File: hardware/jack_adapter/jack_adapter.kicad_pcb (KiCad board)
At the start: 2 copper layers, 25.5 x 22 mm, 3 parts, among them J1 2.5mm Mic, J3 3.5mm Headphones, J4 Conn_01x03

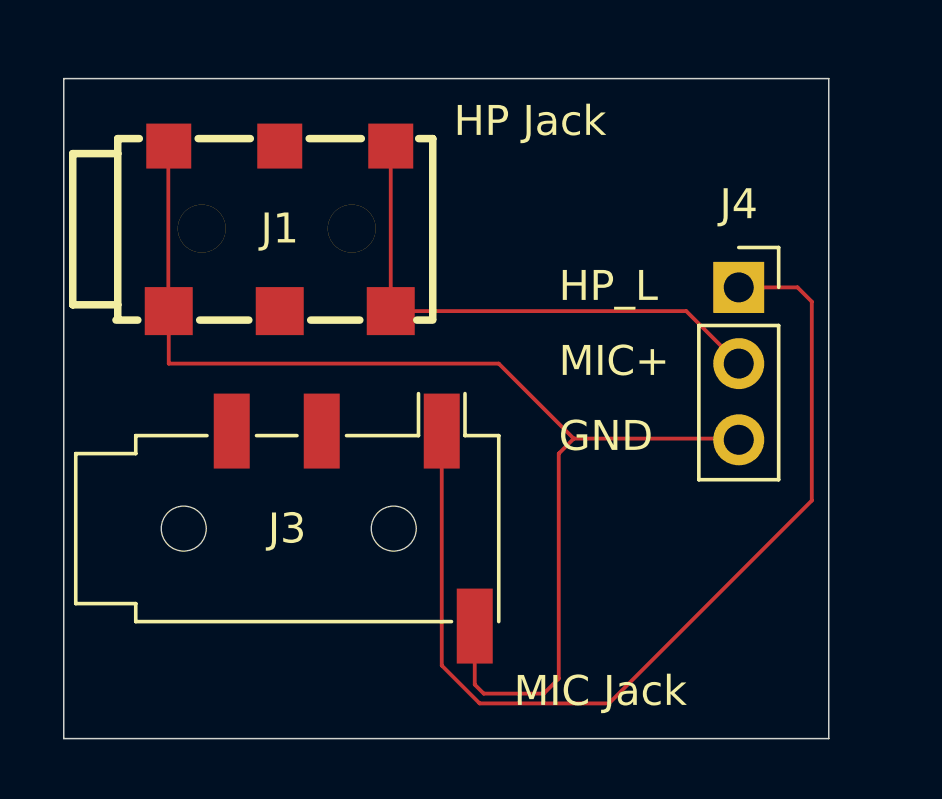
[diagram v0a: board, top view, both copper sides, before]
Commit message: feat: Add audio test circuit and board
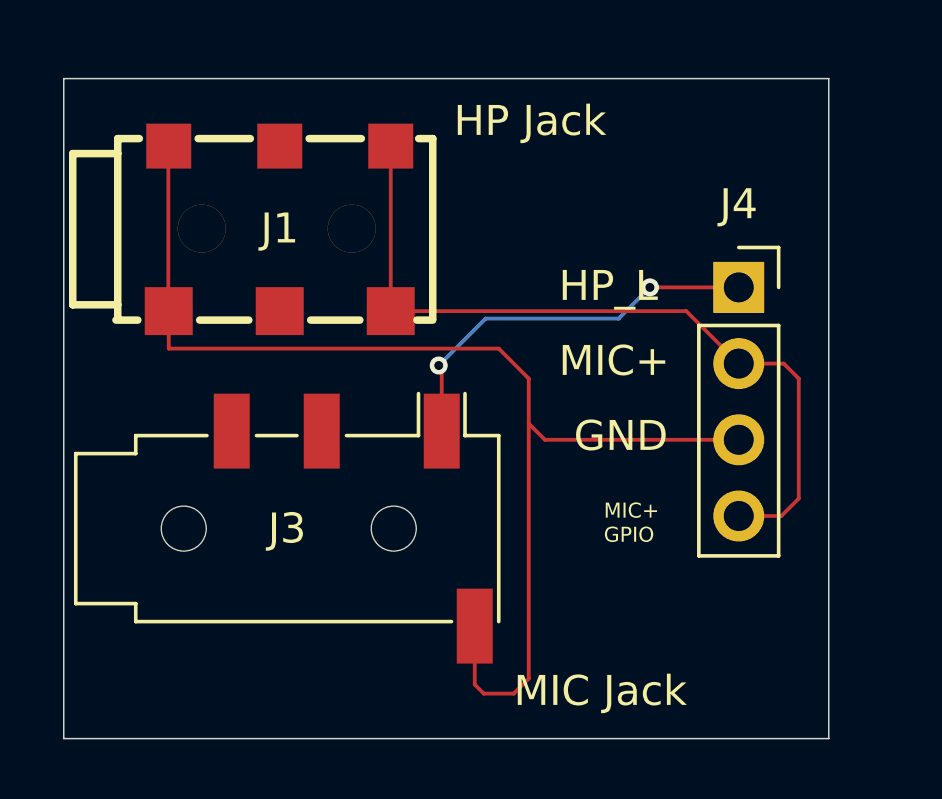
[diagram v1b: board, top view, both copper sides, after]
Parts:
- J4: footprint Connector_PinSocket_2.54mm:PinSocket_1x03_P2.54mm_Vertical -> Connector_PinSocket_2.54mm:PinSocket_1x04_P2.54mm_Vertical
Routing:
- net Net-(J4-Pin_1): track 32.7 -> 13.3 mm, vias 0 -> 2
- net Net-(J4-Pin_2): track 17.8 -> 26.3 mm
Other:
- board text added: "MIC+ GPIO"
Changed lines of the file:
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@@
 		)
 	)
-	(footprint "Connector_PinSocket_2.54mm:PinSocket_1x03_P2.54mm_Vertical"
+	(footprint "Connector_PinSocket_2.54mm:PinSocket_1x04_P2.54mm_Vertical"
 		(layer "F.Cu")
 		(at 37.5 21.96)
-		(descr "Through hole straight socket strip, 1x03, 2.54mm pitch, single row (from Kicad 4.0.7), script generated")
-		(tags "Through hole socket strip THT 1x03 2.54mm single row")
+		(descr "Through hole straight socket strip, 1x04, 2.54mm pitch, single row (from Kicad 4.0.7), script generated")
+		(tags "Through hole socket strip THT 1x04 2.54mm single row")
 		(property "Reference" "J4"
 			(at 0 -2.77 0)
@@
 		)
 		(property "Value" "Conn_01x03"
-			(at 0 7.85 0)
+			(at 0 10.39 0)
 			(layer "F.Fab")
 			(effects
@@
 			)
 		)
-		(property "Description" "Generic connector, single row, 01x03, script generated (kicad-library-utils/schlib/autogen/connector/)"
+		(property "Description" "Generic connector, single row, 01x04, script generated (kicad-library-utils/schlib/autogen/connector/)"
 			(at 0 0 0)
 			(layer "F.Fab")
@@
 		(fp_line
 			(start -1.33 1.27)
-			(end -1.33 6.41)
+			(end -1.33 8.95)
 			(stroke
 				(width 0.12)
@@
 		)
 		(fp_line
-			(start -1.33 6.41)
-			(end 1.33 6.41)
+			(start -1.33 8.95)
+			(end 1.33 8.95)
 			(stroke
 				(width 0.12)
@@
 		(fp_line
 			(start 1.33 1.27)
-			(end 1.33 6.41)
+			(end 1.33 8.95)
 			(stroke
 				(width 0.12)
@@
 		)
 		(fp_line
-			(start -1.8 6.85)
+			(start -1.8 9.4)
 			(end -1.8 -1.8)
 			(stroke
@@
 		(fp_line
 			(start 1.75 -1.8)
-			(end 1.75 6.85)
+			(end 1.75 9.4)
 			(stroke
 				(width 0.05)
@@
 		)
 		(fp_line
-			(start 1.75 6.85)
-			(end -1.8 6.85)
+			(start 1.75 9.4)
+			(end -1.8 9.4)
 			(stroke
 				(width 0.05)
@@
 		)
 		(fp_line
-			(start -1.27 6.35)
+			(start -1.27 8.89)
 			(end -1.27 -1.27)
 			(stroke
@@
 		(fp_line
 			(start 1.27 -0.635)
-			(end 1.27 6.35)
+			(end 1.27 8.89)
 			(stroke
 				(width 0.1)
@@
 		)
 		(fp_line
-			(start 1.27 6.35)
-			(end -1.27 6.35)
+			(start 1.27 8.89)
+			(end -1.27 8.89)
 			(stroke
 				(width 0.1)
@@
 		)
 		(fp_text user "${REFERENCE}"
-			(at 0 2.54 90)
+			(at 0 3.81 90)
 			(layer "F.Fab")
 			(effects
@@
 			(pintype "passive")
 		)
+		(pad "4" thru_hole circle
+			(at 0 7.62)
+			(size 1.7 1.7)
+			(drill 1)
+			(layers "*.Cu" "*.Mask")
+			(remove_unused_layers no)
+			(net 3 "Net-(J4-Pin_2)")
+			(pinfunction "Pin_4")
+			(pintype "passive")
+		)
 		(embedded_fonts no)
-		(model "${KICAD9_3DMODEL_DIR}/Connector_PinSocket_2.54mm.3dshapes/PinSocket_1x03_P2.54mm_Vertical.step"
+		(model "${KICAD9_3DMODEL_DIR}/Connector_PinSocket_2.54mm.3dshapes/PinSocket_1x04_P2.54mm_Vertical.step"
 			(offset
 				(xyz 0 0 0)
@@
 	)
 	(gr_text "GND"
-		(at 31.5 27.5 0)
+		(at 32 27.5 0)
 		(layer "F.SilkS")
 		(effects
@@
 		)
 	)
-	(segment
-		(start 32 27)
-		(end 37.46 27)
-		(width 0.127)
-		(layer "F.Cu")
-		(net 1)
-	)
-	(segment
-		(start 18.5 22.75)
-		(end 18.5 24.5)
+	(gr_text "MIC+\nGPIO"
+		(at 33 30.5 0)
+		(layer "F.SilkS")
+		(effects
+			(font
+				(size 0.5 0.5)
+				(thickness 0.1)
+			)
+			(justify left bottom)
+		)
+	)
+	(segment
+		(start 29.5 24)
+		(end 30.5 25)
+		(width 0.127)
+		(layer "F.Cu")
+		(net 1)
+	)
+	(segment
+		(start 30.5 35)
+		(end 30.5 26.5)
+		(width 0.127)
+		(layer "F.Cu")
+		(net 1)
+	)
+	(segment
+		(start 30 35.5)
+		(end 30.5 35)
 		(width 0.127)
 		(layer "F.Cu")
@@
 	)
 	(segment
+		(start 18.5 24)
+		(end 29.5 24)
+		(width 0.127)
+		(layer "F.Cu")
+		(net 1)
+	)
+	(segment
+		(start 18.5 22.75)
+		(end 18.5 24)
+		(width 0.127)
+		(layer "F.Cu")
+		(net 1)
+	)
+	(segment
 		(start 37.46 27)
 		(end 37.5 27.04)
@@
 	)
 	(segment
-		(start 18.5 24.5)
-		(end 29.5 24.5)
+		(start 28.7 33.25)
+		(end 28.7 35.2)
+		(width 0.127)
+		(layer "F.Cu")
+		(net 1)
+	)
+	(segment
+		(start 29 35.5)
+		(end 30 35.5)
+		(width 0.127)
+		(layer "F.Cu")
+		(net 1)
+	)
+	(segment
+		(start 37.5 27.04)
+		(end 31.04 27.04)
+		(width 0.127)
+		(layer "F.Cu")
+		(net 1)
+	)
+	(segment
+		(start 30.5 25)
+		(end 30.5 26.5)
+		(width 0.127)
+		(layer "F.Cu")
+		(net 1)
+	)
+	(segment
+		(start 18.4855 17.2645)
+		(end 18.4855 22.7355)
+		(width 0.127)
+		(layer "F.Cu")
+		(net 1)
+	)
+	(segment
+		(start 18.4855 22.7355)
+		(end 18.5 22.75)
+		(width 0.127)
+		(layer "F.Cu")
+		(net 1)
+	)
+	(segment
+		(start 31.04 27.04)
+		(end 30.5 26.5)
 		(width 0.127)
 		(layer "F.Cu")
@@
 	)
 	(segment
-		(start 28.7 33.25)
-		(end 28.7 35.2)
-		(width 0.127)
-		(layer "F.Cu")
-		(net 1)
-	)
-	(segment
-		(start 29.5 24.5)
-		(end 32 27)
-		(width 0.127)
-		(layer "F.Cu")
-		(net 1)
-	)
-	(segment
-		(start 31.5 27.5)
-		(end 32 27)
-		(width 0.127)
-		(layer "F.Cu")
-		(net 1)
-	)
-	(segment
-		(start 31 35.5)
-		(end 31.5 35)
-		(width 0.127)
-		(layer "F.Cu")
-		(net 1)
-	)
-	(segment
-		(start 29 35.5)
-		(end 31 35.5)
-		(width 0.127)
-		(layer "F.Cu")
-		(net 1)
-	)
-	(segment
-		(start 18.4855 17.2645)
-		(end 18.4855 22.7355)
-		(width 0.127)
-		(layer "F.Cu")
-		(net 1)
-	)
-	(segment
-		(start 18.4855 22.7355)
-		(end 18.5 22.75)
-		(width 0.127)
-		(layer "F.Cu")
-		(net 1)
-	)
-	(segment
-		(start 31.5 35)
-		(end 31.5 27.5)
-		(width 0.127)
-		(layer "F.Cu")
-		(net 1)
-	)
-	(segment
-		(start 27.6 26.75)
-		(end 27.6 34.563862)
+		(start 34.54 21.96)
+		(end 37.5 21.96)
 		(width 0.127)
 		(layer "F.Cu")
@@
 	)
 	(segment
-		(start 28.864138 35.828)
-		(end 33.172 35.828)
+		(start 27.6 24.6635)
+		(end 27.6 26.75)
 		(width 0.127)
 		(layer "F.Cu")
@@
 	)
 	(segment
-		(start 39.9355 29.0645)
-		(end 39.9355 22.4355)
+		(start 27.5 24.5635)
+		(end 27.6 24.6635)
 		(width 0.127)
 		(layer "F.Cu")
 		(net 2)
 	)
-	(segment
-		(start 39.46 21.96)
-		(end 37.5 21.96)
-		(width 0.127)
-		(layer "F.Cu")
+	(via
+		(at 34.54 21.96)
+		(size 0.6)
+		(drill 0.3)
+		(layers "F.Cu" "B.Cu")
 		(net 2)
 	)
-	(segment
-		(start 33.172 35.828)
-		(end 39.9355 29.0645)
-		(width 0.127)
-		(layer "F.Cu")
+	(via
+		(at 27.5 24.5635)
+		(size 0.6)
+		(drill 0.3)
+		(layers "F.Cu" "B.Cu")
 		(net 2)
 	)
 	(segment
-		(start 27.6 34.563862)
-		(end 28.864138 35.828)
-		(width 0.127)
-		(layer "F.Cu")
+		(start 29.0635 23)
+		(end 33.5 23)
+		(width 0.127)
+		(layer "B.Cu")
 		(net 2)
 	)
 	(segment
-		(start 39.9355 22.4355)
-		(end 39.46 21.96)
-		(width 0.127)
-		(layer "F.Cu")
+		(start 27.5 24.5635)
+		(end 29.0635 23)
+		(width 0.127)
+		(layer "B.Cu")
 		(net 2)
+	)
+	(segment
+		(start 33.5 23)
+		(end 34.54 21.96)
+		(width 0.127)
+		(layer "B.Cu")
+		(net 2)
+	)
+	(segment
+		(start 38.92 29.58)
+		(end 37.5 29.58)
+		(width 0.127)
+		(layer "F.Cu")
+		(net 3)
 	)
 	(segment
@@
 	)
 	(segment
+		(start 37.5 24.5)
+		(end 39 24.5)
+		(width 0.127)
+		(layer "F.Cu")
+		(net 3)
+	)
+	(segment
+		(start 39 24.5)
+		(end 39.5 25)
+		(width 0.127)
+		(layer "F.Cu")
+		(net 3)
+	)
+	(segment
+		(start 39.5 25)
+		(end 39.5 29)
+		(width 0.127)
+		(layer "F.Cu")
+		(net 3)
+	)
+	(segment
 		(start 35.75 22.75)
 		(end 37.5 24.5)
@@
 		(width 0.127)
 		(layer "F.Cu")
+		(net 3)
+	)
+	(segment
+		(start 39.5 29)
+		(end 38.92 29.58)
+		(width 0.127)
+		(layer "F.Cu")

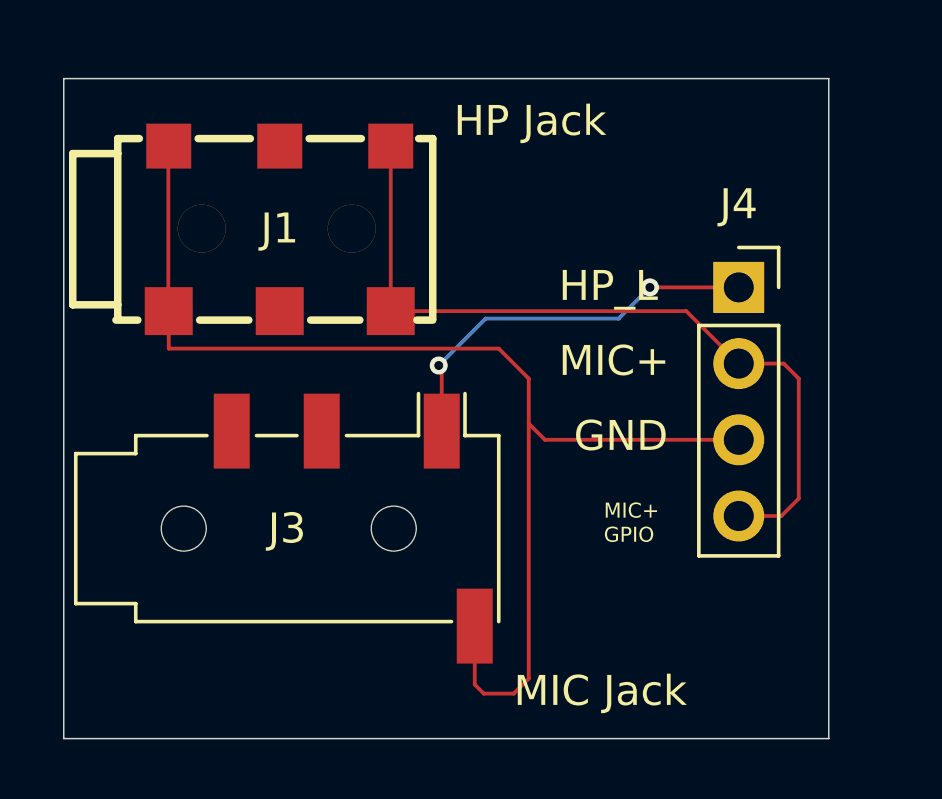
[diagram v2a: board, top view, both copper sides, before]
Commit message: feat: Added in voltage divider and diode to detect ptt from midlands headset
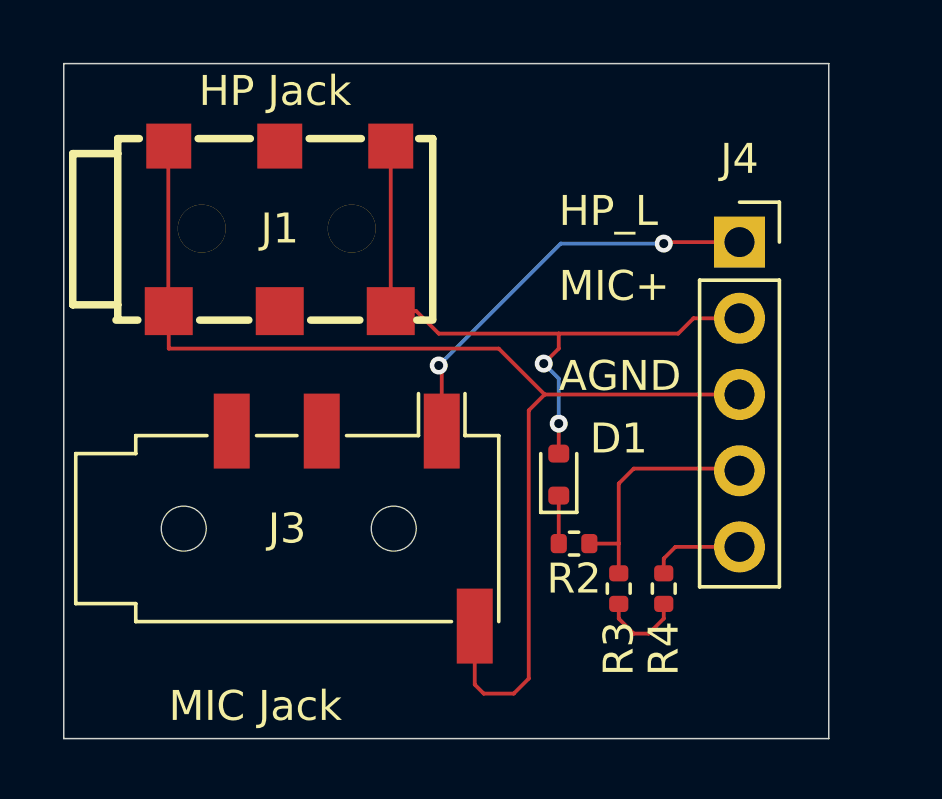
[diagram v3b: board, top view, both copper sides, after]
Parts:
- added D1: 1N4148WT, Diode_SMD:D_SOD-523, F.Cu at (31.5, 28.2)
- added R2: 50k, Resistor_SMD:R_0402_1005Metric, F.Cu at (32.0, 30.5)
- added R3: 100k, Resistor_SMD:R_0402_1005Metric, F.Cu at (33.5, 32.0)
- added R4: 10k, Resistor_SMD:R_0402_1005Metric, F.Cu at (35.0, 32.0)
- J4: value Conn_01x03 -> Header; footprint Connector_PinSocket_2.54mm:PinSocket_1x04_P2.54mm_Vertical -> Connector_PinSocket_2.54mm:PinSocket_1x05_P2.54mm_Vertical
- moved J4 1.51 mm to (37.5, 20.4)
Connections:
- J1 pad T: Net-(J4-Pin_2) -> Net-(D1-A)
- J4 pad 2: Net-(J4-Pin_2) -> Net-(D1-A)
- J4 pad 4: Net-(J4-Pin_2) -> Net-(J4-Pin_4)
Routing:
- net Net-(J4-Pin_2): track 26.3 -> 0.00 mm
- net Net-(D1-A): track 0.00 -> 22.1 mm, vias 0 -> 2
- net Net-(J4-Pin_4): track 0.00 -> 8.23 mm
- net Net-(J4-Pin_5): track 0.00 -> 3.18 mm
- net Net-(R3-Pad2): track 0.00 -> 2.89 mm
- net Net-(D1-K): track 0.00 -> 1.60 mm
- net Net-(J4-Pin_1): track 13.3 -> 14.0 mm
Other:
- board size 25.5 x 22 mm -> 25.5 x 22.5 mm
- board text added: "AGND"
- board text removed: "GND"
- board text removed: "MIC+ GPIO"

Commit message: feat: Moved the jacks slightly to be inline diagonally
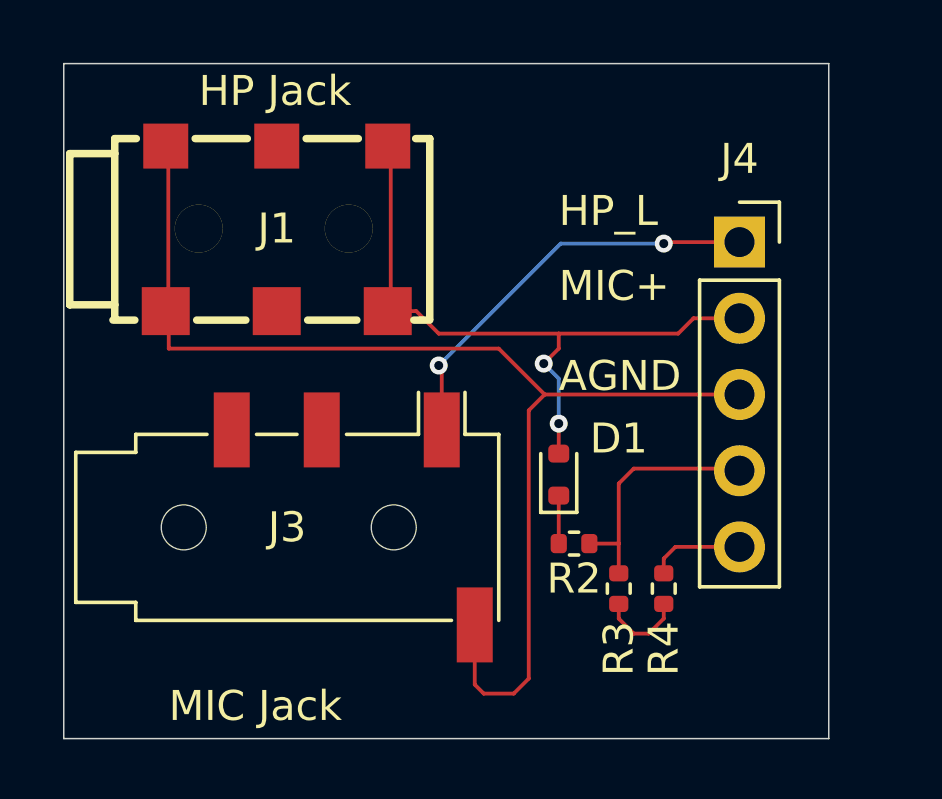
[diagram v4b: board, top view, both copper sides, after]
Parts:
- moved J1 0.10 mm to (22.1, 20.0)
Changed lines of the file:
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@@
 	(footprint "Connector_Audio:Jack_3.5mm_PJ320D_Horizontal"
 		(layer "F.Cu")
-		(at 23.775 30)
+		(at 23.775 29.95942)
 		(descr "Headphones with microphone connector, 3.5mm, 4 pins (http://www.qingpu-electronics.com/en/products/WQP-PJ320D-72.html)")
 		(tags "3.5mm jack mic microphone phones headphones 4pins audio plug")
@@
 	(footprint "hactar_lib:AUDIO-SMD_PJ-242D-SMT"
 		(layer "F.Cu")
-		(at 22.2 20)
+		(at 22.1 20)
 		(property "Reference" "J1"
 			(at 0 0 0)
@@
 			)
 		)
-		(property "JLCPCB Part #" "C431535"
+		(property "JLCPCB Part #" "C431536"
 			(at 0 0 0)
 			(unlocked yes)
@@
 	)
 	(segment
-		(start 30.5 35)
-		(end 30.5 26.06)
-		(width 0.127)
-		(layer "F.Cu")
-		(net 1)
-	)
-	(segment
-		(start 30 35.5)
-		(end 30.5 35)
-		(width 0.127)
-		(layer "F.Cu")
-		(net 1)
-	)
-	(segment
 		(start 31.03 25.53)
 		(end 37.525 25.53)
@@
 	)
 	(segment
-		(start 30.5 26.06)
-		(end 31.03 25.53)
+		(start 28.7 35.2)
+		(end 29 35.5)
+		(width 0.127)
+		(layer "F.Cu")
+		(net 1)
+	)
+	(segment
+		(start 29 35.5)
+		(end 30 35.5)
 		(width 0.127)
 		(layer "F.Cu")
@@
 	)
 	(segment
+		(start 30.5 26.06)
+		(end 31.03 25.53)
+		(width 0.127)
+		(layer "F.Cu")
+		(net 1)
+	)
+	(segment
+		(start 30.5 35)
+		(end 30.5 26.06)
+		(width 0.127)
+		(layer "F.Cu")
+		(net 1)
+	)
+	(segment
 		(start 18.4855 17.2645)
 		(end 18.4855 22.7355)
@@
 	)
 	(segment
+		(start 29.5 24)
+		(end 31.03 25.53)
+		(width 0.127)
+		(layer "F.Cu")
+		(net 1)
+	)
+	(segment
 		(start 28.7 33.25)
 		(end 28.7 35.2)
@@
 	)
 	(segment
-		(start 29.5 24)
-		(end 31.03 25.53)
+		(start 30 35.5)
+		(end 30.5 35)
 		(width 0.127)
 		(layer "F.Cu")
-		(net 1)
-	)
-	(segment
-		(start 28.7 35.2)
-		(end 29 35.5)
-		(width 0.127)
-		(layer "F.Cu")
-		(net 1)
-	)
-	(segment
-		(start 29 35.5)
-		(end 30 35.5)
-		(width 0.127)
-		(layer "F.Cu")

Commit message: feat: Changed resistor part number, and jumpers, and re-arranged things a bit
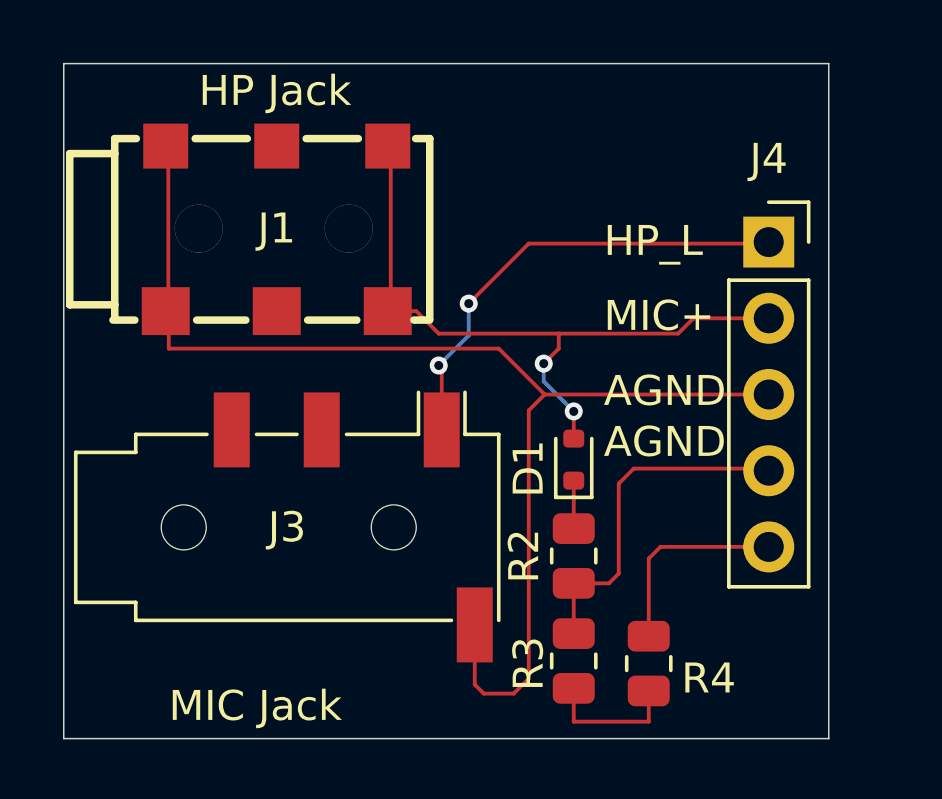
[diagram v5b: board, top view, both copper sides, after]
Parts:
- R2: value 50k -> 51k; footprint Resistor_SMD:R_0402_1005Metric -> Resistor_SMD:R_0805_2012Metric
- R3, R4: footprint Resistor_SMD:R_0402_1005Metric -> Resistor_SMD:R_0805_2012Metric
- moved R3 2.84 mm to (32.0, 34.4)
- moved R4 2.55 mm to (34.5, 34.5)
- moved J4 0.98 mm to (38.5, 20.4)
- moved D1 0.71 mm to (32.0, 27.7)
- moved R2 0.41 mm to (32.0, 30.9), turned to 90 degrees
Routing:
- net Net-(J4-Pin_5): track 3.18 -> 6.75 mm
- net Net-(J4-Pin_4): track 8.23 -> 11.5 mm
- net Net-(R3-Pad2): track 2.89 -> 4.63 mm
- net Net-(J4-Pin_1): track 14.0 -> 15.6 mm
- net Net-(J4-Pin_3): track 40.2 -> 41.2 mm
- net Net-(D1-A): track 22.1 -> 22.7 mm

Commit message: chore: fix misaligned 2.5mm jack
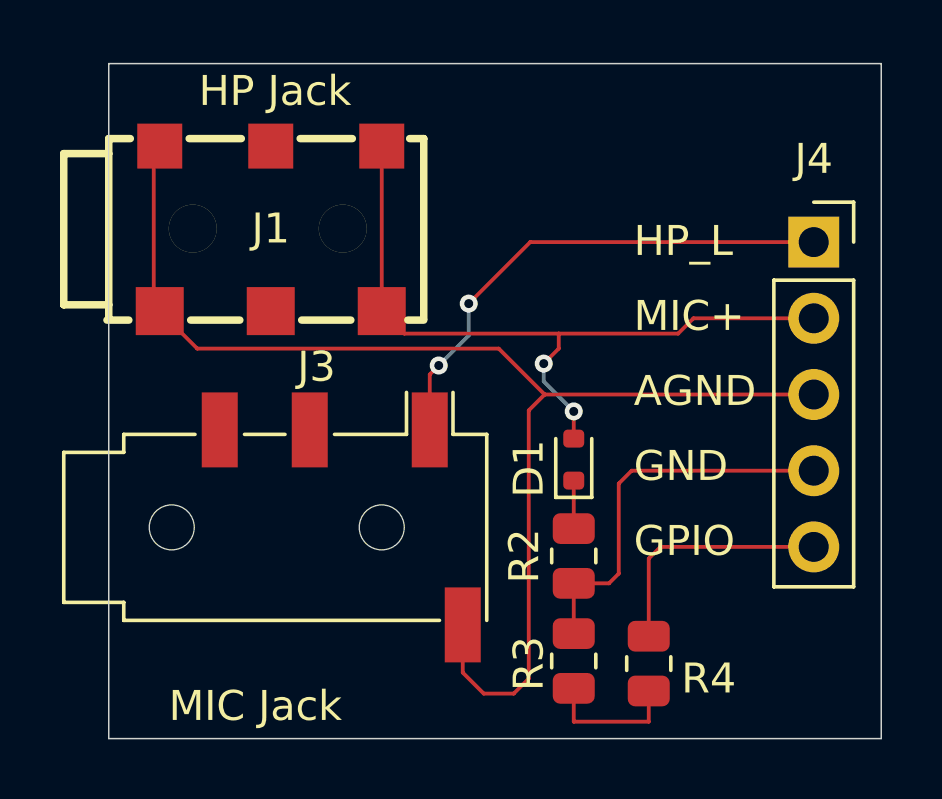
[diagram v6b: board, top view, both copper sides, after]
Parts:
- J3: footprint Connector_Audio:Jack_3.5mm_PJ320D_Horizontal -> hactar_lib:Jack_3.5mm_PJ320D_Horizontal
- moved J4 1.50 mm to (40.0, 20.4)
- moved J3 0.57 mm to (23.2, 30.0)
- moved J1 0.20 mm to (21.9, 20.0)
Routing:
- net Net-(D1-A): track 22.7 -> 24.7 mm
- net Net-(J4-Pin_1): track 15.6 -> 17.3 mm
- net Net-(J4-Pin_3): track 41.2 -> 42.8 mm
- net Net-(J4-Pin_5): track 6.75 -> 8.25 mm
- net Net-(J4-Pin_4): track 11.5 -> 13.0 mm
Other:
- board size 25.5 x 22.5 mm -> 25.8 x 22.5 mm
- board text added: "GND"
- board text added: "GPIO"
